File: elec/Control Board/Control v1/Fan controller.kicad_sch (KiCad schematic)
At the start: 24 parts, among them J10 Conn_01x05, J11 Conn_01x04, J12 Conn_01x07, J13 Screw_Terminal_01x02, J21 Conn_01x04_Pin, J6 DB25_Female_MountingHoles, J9 Conn_01x04, Q12 NCE01P30K, Q601 BSS138

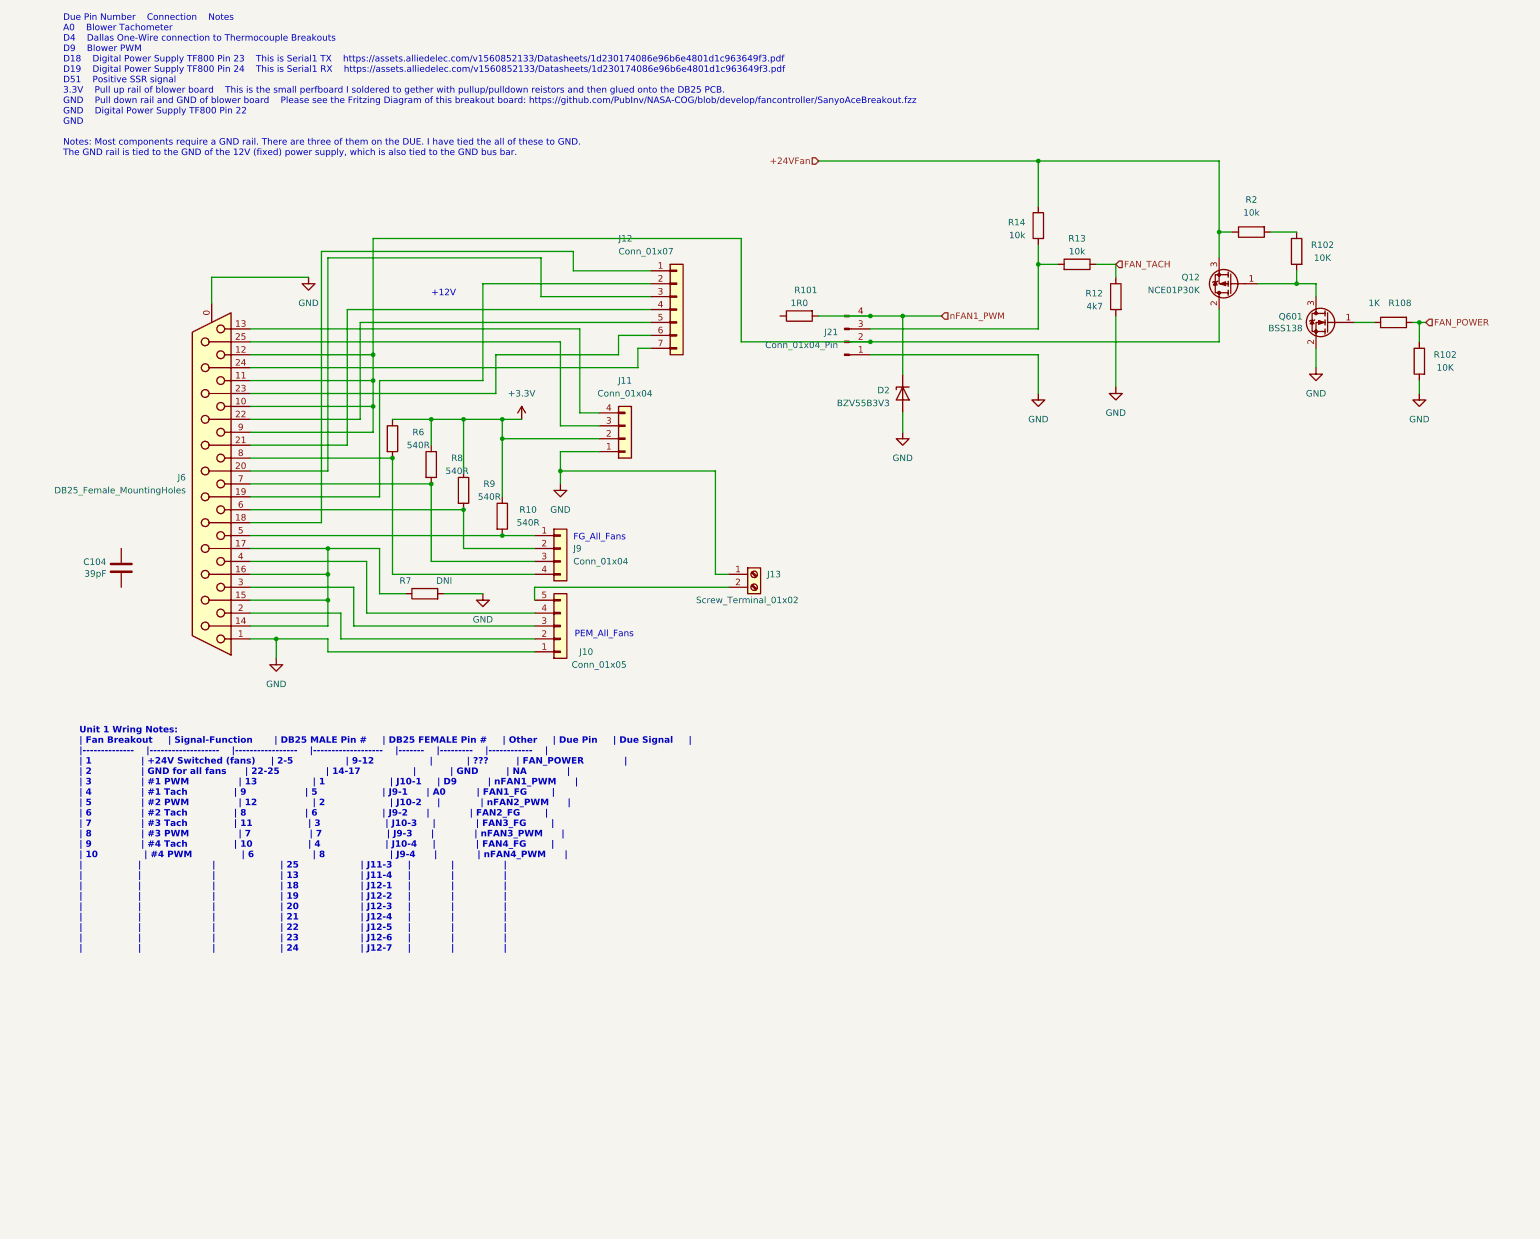
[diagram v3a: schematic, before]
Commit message: Complete Fan1 PWM control. Fan1 Tach / FG.
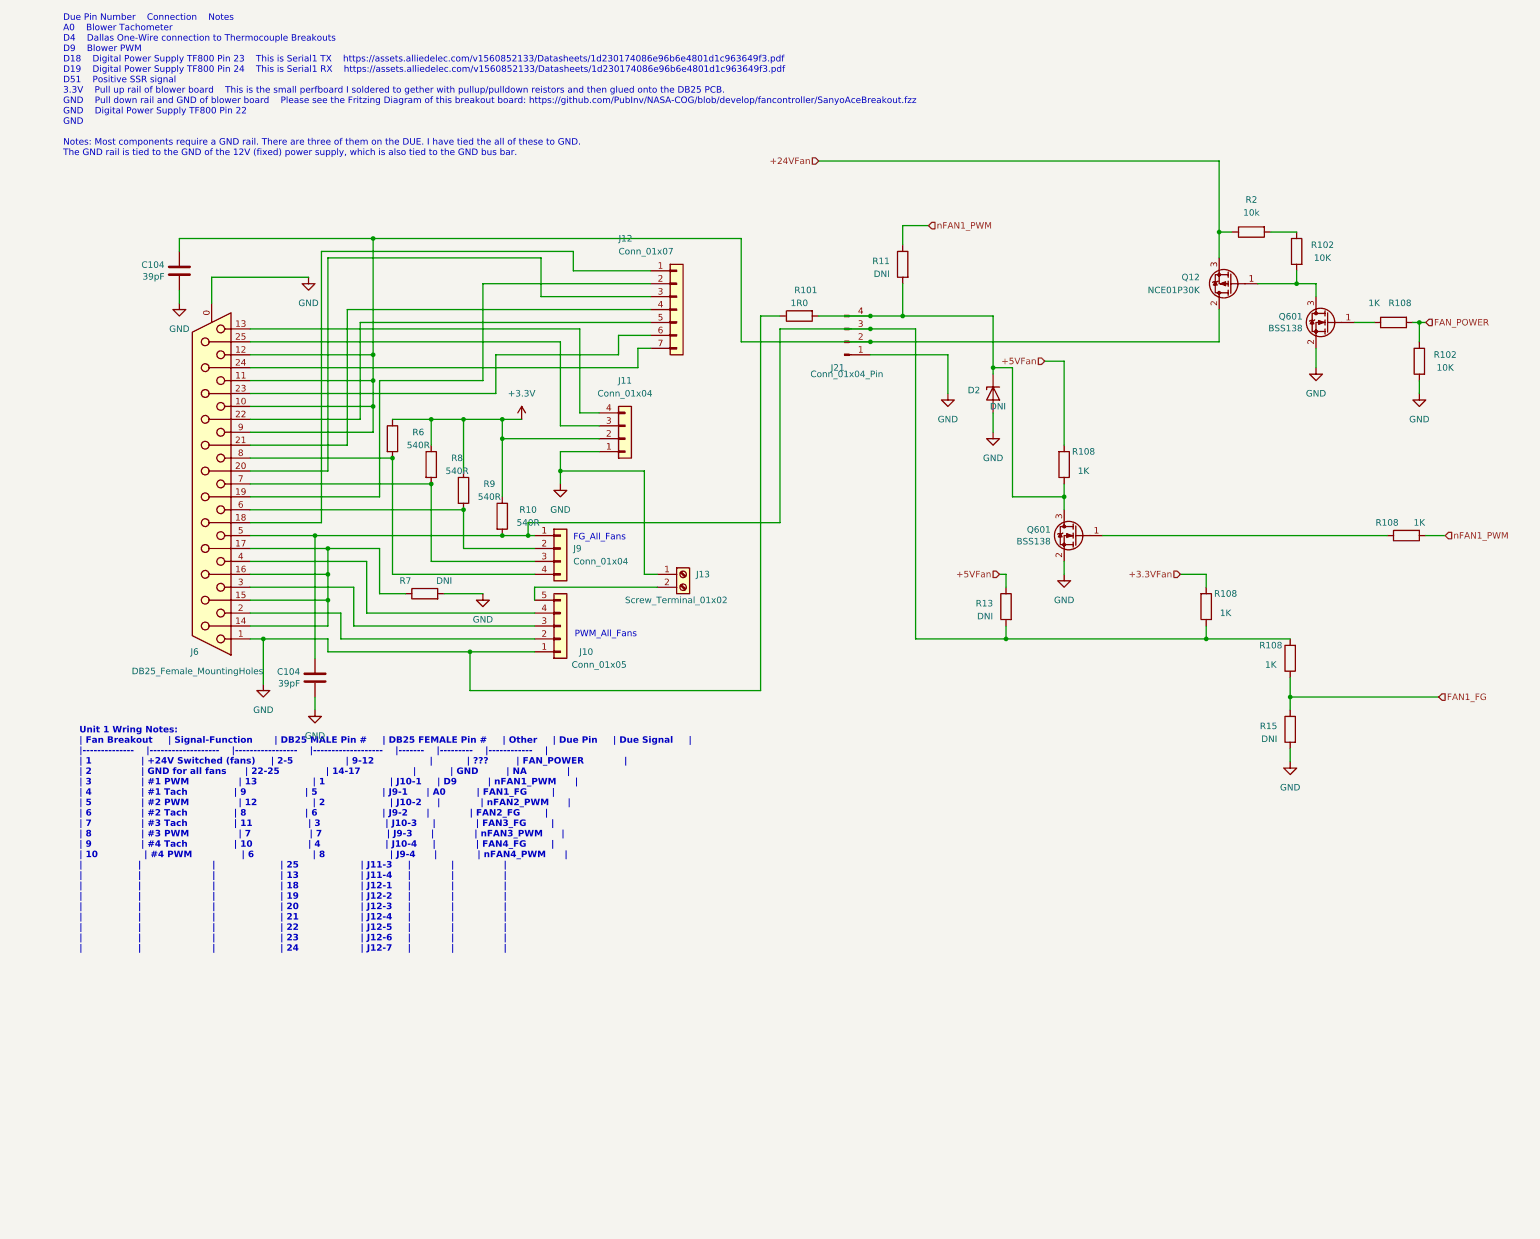
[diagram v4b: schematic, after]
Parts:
- removed R12: 4k7, symbol Device:R
- removed R14: 10k, symbol Device:R
- added C104: 39pF, Capacitor_SMD:C_0603_1608Metric_Pad1.08x0.95mm_HandSolder, symbol Device:C
- added Q601: BSS138, Package_TO_SOT_SMD:SOT-23, symbol Transistor_FET:BSS138
- added R108 (x4): 1K, Resistor_SMD:R_0603_1608Metric_Pad0.98x0.95mm_HandSolder, symbol Device:R
- added R11: DNI, Resistor_SMD:R_0603_1608Metric_Pad0.98x0.95mm_HandSolder, symbol Device:R
- added R15: DNI, symbol Device:R
- D2: value BZV55B3V3 -> DNI
- R13: value 10k -> DNI
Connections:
- net GND: now also C104.2, R101.1, C104.2, Q601.2 (S), R15.2
- net nFAN1_PWM: now also R108.2, R11.1; no longer D2.1 (K), J21.4 (Pin_4), R101.2
- net at J6.5, J9.1 (Pin_1), R10.2: now also J21.3 (Pin_3), R13.2, C104.1, R108.1, R108.2
- net at J21.2 (Pin_2), J6.10, J6.11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: now also C104.1
- net FAN_TACH renamed +5VFan
- net +5VFan: now also R108.2
- new net: D2.1 (K), J21.4 (Pin_4), Q601.3 (D), R101.2, R108.1, R11.2
- new net: Q601.1 (G), R108.1
- new net +3.3VFan: R108.2
- new net FAN1_FG: R108.1, R15.1
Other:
- note added: "PWM_All_Fans"
- note removed: "+12V"
- note removed: "PEM_All_Fans"
- moved on the sheet: C104, D2, J13
